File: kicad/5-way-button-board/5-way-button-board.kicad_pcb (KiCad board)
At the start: 2 copper layers, 44 x 40 mm, 12 parts, among them J1 Conn_01x06_Pin, J2 Conn_01x06_Pin, SW6 SW_Push_LEDx5

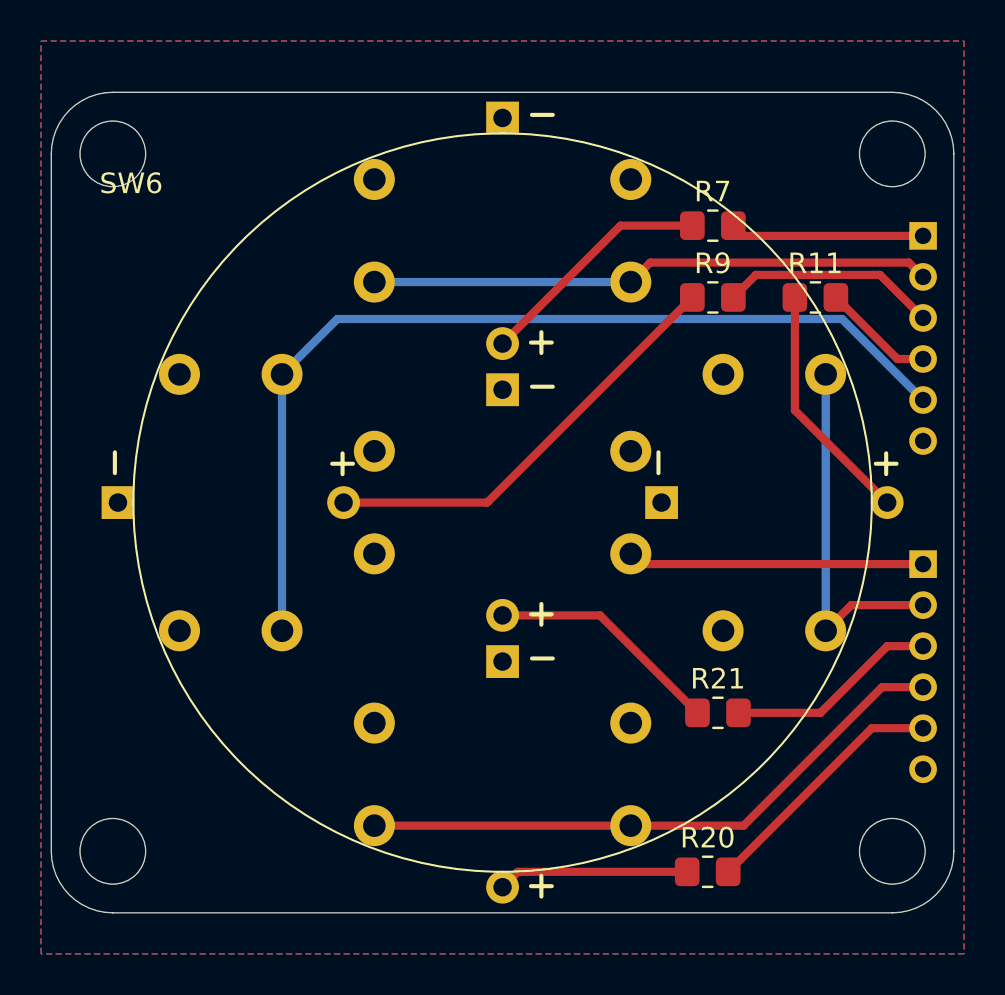
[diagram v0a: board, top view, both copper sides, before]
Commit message: Add encoder board
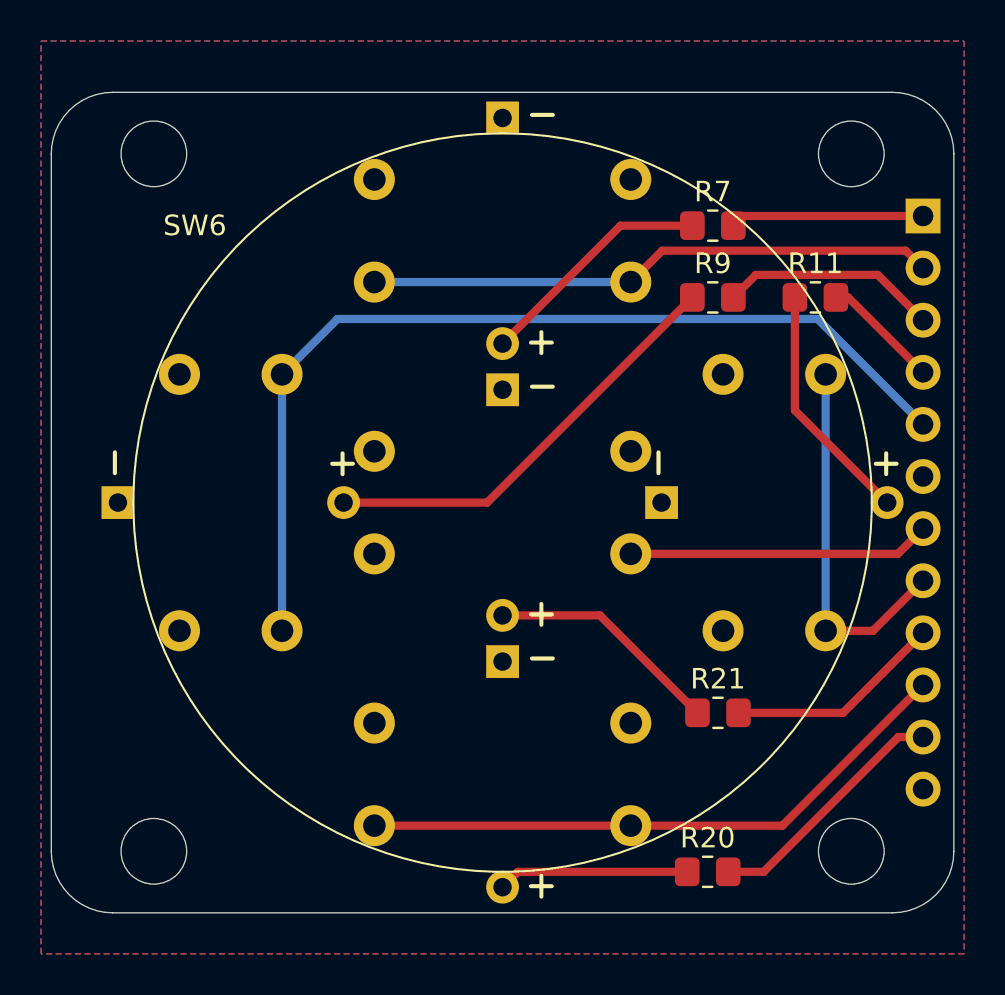
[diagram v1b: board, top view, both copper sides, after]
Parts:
- removed J1, J2: Conn_01x06_Pin, Connector_PinHeader_2.00mm:PinHeader_1x06_P2.00mm_Vertical
- added J3: Conn_01x12_Pin, Connector_PinHeader_2.54mm:PinHeader_1x12_P2.54mm_Vertical, B.Cu at (170.5, 86.0)
- moved H1 2.00 mm to (133.0, 83.0)
- moved H2 2.00 mm to (167.0, 83.0)
- moved H3 2.00 mm to (133.0, 117.0)
- moved H4 2.00 mm to (167.0, 117.0)

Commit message: PCB trace finished
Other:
- board text added: "2026.05.29"
- board text added: "github.com/mar0x/midi_controller"
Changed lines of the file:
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@@
 		(layer "Edge.Cuts")
+	)
+	(gr_text "github.com/mar0x/midi_controller"
+		(at 151.23 113.64 0)
+		(layer "B.SilkS")
+		(effects
+			(font
+				(size 0.8 0.8)
+				(thickness 0.1)
+			)
+			(justify left bottom mirror)
+		)
+	)
+	(gr_text "2026.05.29"
+		(at 139.24 112.2 0)
+		(layer "B.SilkS")
+		(effects
+			(font
+				(size 1 1)
+				(thickness 0.2)
+				(bold yes)
+			)
+			(justify left bottom mirror)
+		)
 	)
 	(segment
